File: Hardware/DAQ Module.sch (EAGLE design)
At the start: 31 parts, among them IC2 LM4040AIM3-2.0_NOPB, J1 393570014, J2 MF-CON-2.54mm-01x06, J3 393570014, J4 MF-CON-2.54mm-01x06, J5 MF-CON-2.54mm-01x06, J6 UJ2-MIBH2-4-SMT-TR, SW1 SPST_TACT-KMR2, U1 ATMEGA32U4TQFP, Y1 16MHz

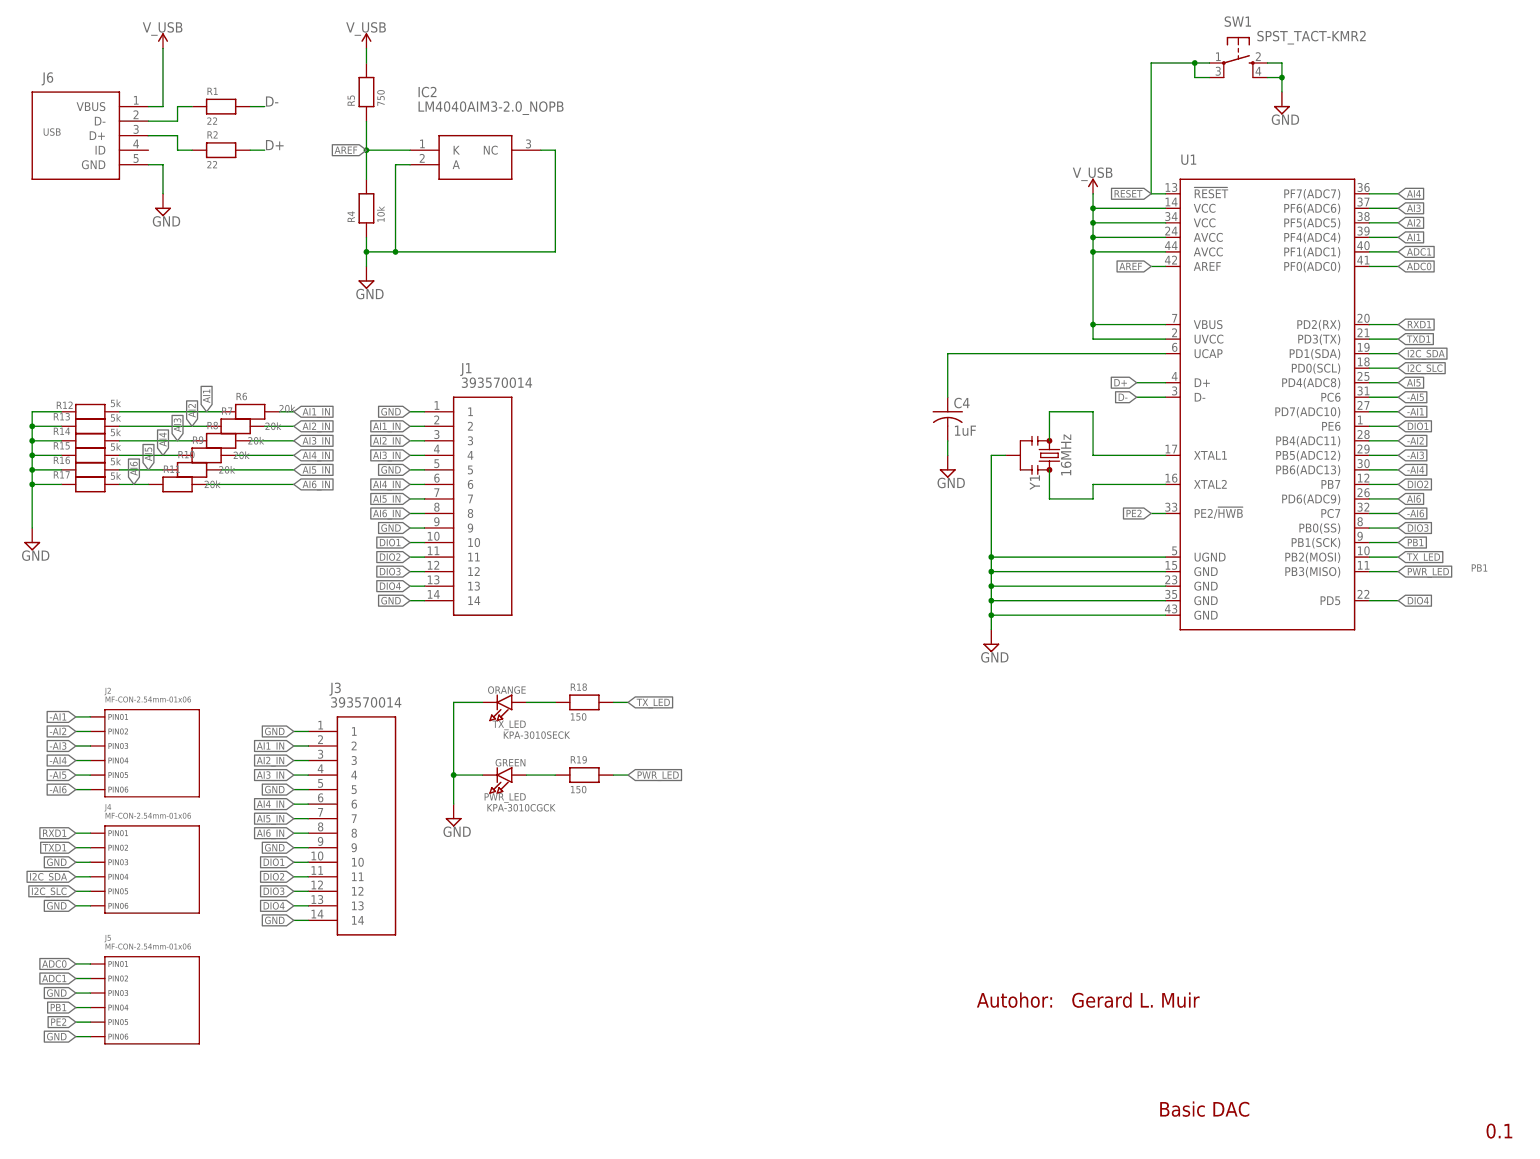
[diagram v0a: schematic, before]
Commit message: Hardware updates.
- Remapping of ports for easier prototyping.
- Addition of serial programming port.
- New smaller board layout.
- Higher analog imput impedance.
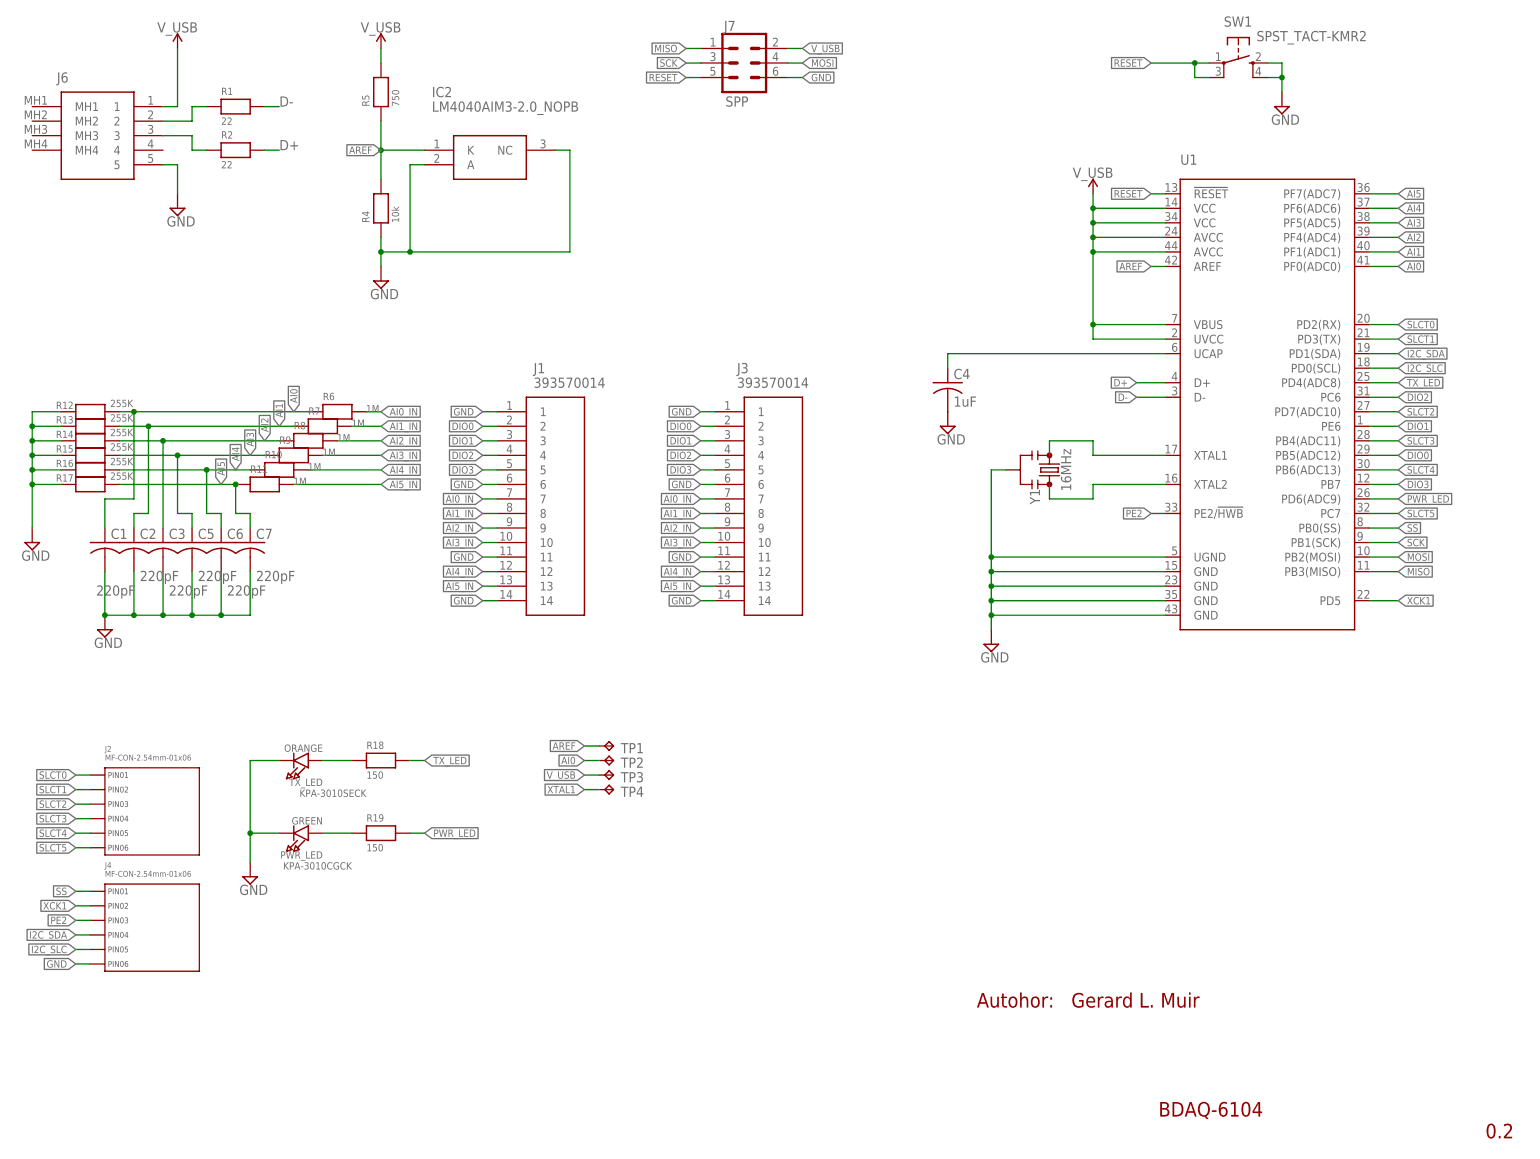
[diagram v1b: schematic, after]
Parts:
- removed J5: MF-CON-2.54mm-01x06, MF_Connectors:CON_01X06_PTH_2.54MM
- added C1, C2, C3, C5, C6, C7: 220pF, adafruit:C-USC1206
- added J7: SPP, SparkFun-Connectors:CONN_03X2FEMALE
- added TP1, TP2, TP3, TP4: TPB1,27, testpad:TPB1,27
- R10, R11, R7, R8, R9: value 20k -> 1M; MANUFACTURER_NAME (none) -> Stackpole Electronics Inc; MANUFACTURER_PART (none) -> RNCS1206BKE1M00; SUPPLIER (none) -> NEWARK; SUPPLIER_PART (none) -> RNCS1206BKE1M00TR-ND
- R12: value 5k -> 255K; MANUFACTURER_NAME MULTICOMP PRO -> Panasonic; MANUFACTURER_PART MC009150 -> ERA-8AEB2553V; SUPPLIER_PART 79AC2429 -> P255KBCCT-ND
- R13, R14, R15, R16, R17: value 5k -> 255K; MANUFACTURER_NAME (none) -> Panasonic; MANUFACTURER_PART (none) -> ERA-8AEB2553V; SUPPLIER (none) -> NEWARK; SUPPLIER_PART (none) -> P255KBCCT-ND
- R6: value 20k -> 1M; MANUFACTURER_NAME YAGEO -> Stackpole Electronics Inc; MANUFACTURER_PART RP1206BRD0720KL -> RNCS1206BKE1M00; SUPPLIER_PART 61AK7932 -> RNCS1206BKE1M00TR-ND
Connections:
- net -AI6 renamed SLCT5
- net N$4 renamed XTAL2
- removed net -AI1: J2.PIN1, U1.PD7(ADC10)
- removed net -AI2: J2.PIN2, U1.PB4(ADC11)
- removed net -AI3: J2.PIN3, U1.PB5(ADC12)
- removed net -AI4: J2.PIN4, U1.PB6(ADC13)
- removed net -AI5: J2.PIN5, U1.PC6
- removed net ADC0: J5.PIN1, U1.PF0(ADC0)
- removed net ADC1: J5.PIN2, U1.PF1(ADC1)
- removed net AI6: R11.1, R17.2, U1.PD6(ADC9)
- removed net AI6_IN: J1.8, J3.8, R11.2
- removed net DIO4: J1.13, J3.13, U1.PD5
- removed net N$3: U1.XTAL1, Y1.3
- removed net PB1: J5.PIN4, U1.PB1(SCK)
- removed net RXD1: J4.PIN1, U1.PD2(RX)
- removed net TXD1: J4.PIN2, U1.PD3(TX)
- new net AI0: C1.1, R12.2, R6.1, TP2.TP, U1.PF0(ADC0)
- new net AI0_IN: J1.7, J3.7, R6.2
- new net DIO0: J1.2, J3.2, U1.PB5(ADC12)
- new net MISO: J7.1, U1.PB3(MISO)
- new net MOSI: J7.4, U1.PB2(MOSI)
- new net SCK: J7.3, U1.PB1(SCK)
- new net SLCT0: J2.PIN1, U1.PD2(RX)
- new net SLCT1: J2.PIN2, U1.PD3(TX)
- new net SLCT2: J2.PIN3, U1.PD7(ADC10)
- new net SLCT3: J2.PIN4, U1.PB4(ADC11)
- new net SLCT4: J2.PIN5, U1.PB6(ADC13)
- new net SS: J4.PIN1, U1.PB0(SS)
- new net XCK1: J4.PIN2, U1.PD5
- new net XTAL1: TP4.TP, U1.XTAL1, Y1.3
- net AI1: now also C2.1, R13.2, R7.1, U1.PF1(ADC1); no longer R12.2, R6.1, U1.PF4(ADC4)
- net AI1_IN: now also J1.8, J3.8, R7.2; no longer J1.2, J3.2, R6.2
- net AI2: now also C3.1, R14.2, R8.1, U1.PF4(ADC4); no longer R13.2, R7.1, U1.PF5(ADC5)
- net AI2_IN: now also J1.9, J3.9, R8.2; no longer J1.3, J3.3, R7.2
- net AI3: now also C5.1, R15.2, R9.1, U1.PF5(ADC5); no longer R14.2, R8.1, U1.PF6(ADC6)
- net AI3_IN: now also J1.10, J3.10, R9.2; no longer J1.4, J3.4, R8.2
- net AI4: now also C6.1, R10.1, R16.2, U1.PF6(ADC6); no longer R15.2, R9.1, U1.PF7(ADC7)
- net AI4_IN: now also J1.12, J3.12, R10.2; no longer J1.6, J3.6, R9.2
- net AI5: now also C7.1, R11.1, R17.2, U1.PF7(ADC7); no longer R10.1, R16.2, U1.PD4(ADC8)
- net AI5_IN: now also J1.13, J3.13, R11.2; no longer J1.7, J3.7, R10.2
- net AREF: now also TP1.TP
- net DIO1: now also J1.3, J3.3; no longer J1.10, J3.10
- net DIO2: now also J1.4, J3.4, U1.PC6; no longer J1.11, J3.11, U1.PB7
- net DIO3: now also J1.5, J3.5, U1.PB7; no longer J1.12, J3.12, U1.PB0(SS)
- net GND: now also C1.2, C2.2, C3.2, C5.2, C6.2, C7.2, J1.11, J1.6, J3.11, J3.6, J6.5, J7.6; no longer J1.5, J1.9, J3.5, J3.9, J4.PIN3, J5.PIN3, J5.PIN6, J6.GND
- net N$2: now also J6.2; no longer J6.D-
- net N$5: now also J6.3; no longer J6.D+
- net PE2: now also J4.PIN3; no longer J5.PIN5
- net PWR_LED: now also U1.PD6(ADC9); no longer U1.PB3(MISO)
- net RESET: now also J7.5
- net TX_LED: now also U1.PD4(ADC8); no longer U1.PB2(MOSI)
- net V_USB: now also J6.1, J7.2, TP3.TP; no longer J6.VBUS
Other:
- note added: "0.2"
- note added: "BDAQ-6104"
- note removed: "0.1"
- note removed: "Basic DAC"
- moved on the sheet: C4, IC2, J1, J2, J3, J4, PWR_LED, R1, R10, R11, R18, R19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

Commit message: Hardware updates and corresponding SW updates.
- Updated analog input circuitry to use a 4.096 ARef.
- Added analog input filtering.
- Updated firmware to utilize new analog input circuitry.
- Some general clean up of firmware.
- Updated examples in LabView driver.
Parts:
- C1, C2, C3, C5, C6, C7: value 220pF -> 470pF; MANUFACTURER_PART C1206C221J1HACAUTO -> C1206C471J5GACTU; SUPPLIER_PART 399-C1206C221J1HACAUTOCT-ND -> 50AC8485
- IC2: value LM4040AIM3-2.0_NOPB -> LM4040AIM3-4.1_NOPB; device LM4040AIM3-2.0_NOPB:LM4040AIM3-2.0_NOPB -> LM4040AIM3-4.1_NOPB:LM4040AIM3-4.1_NOPB
- R10, R11, R6, R7, R8, R9: value 1M -> 590K; device microbuilder:RESISTOR1206 -> ERJ3RED5903V:ERJ3RED5903V
- R12, R13, R14, R15, R16, R17: value 255K -> 402K; MANUFACTURER_NAME Panasonic -> MULTICOMP PRO; MANUFACTURER_PART ERA-8AEB2553V -> MCWF12R4023BTL; SUPPLIER_PART P255KBCCT-ND -> 92AH9453
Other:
- moved on the sheet: J1, J2, J3, J4, PWR_LED, R18, R19, TP1, TP2, TP3, TP4, TX_LED
